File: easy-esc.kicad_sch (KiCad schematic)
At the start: 43 parts, among them J101 USB_C_Receptacle_USB2.0, J102 BLDC, J103 POWER, SW101 BOOT, SW102 RESET, SW103 EN, U101 TMC6300, U102 XC6206, U103 W25Q128JVS, U104 RP2040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

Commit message: finalize fab files
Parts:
- added C113: 100uF, Capacitor_SMD:CP_Elec_4x3.9, symbol Device:C_Polarized_US
- added H101: PCB, matei:easy-esc-outline, symbol Mechanical:MountingHole_Pad
- added R113, R114: 0, Resistor_SMD:R_0402_1005Metric, symbol Device:R_Small_US
- added U105, U106: INA180A1, Package_TO_SOT_SMD:SOT-23-5, symbol Amplifier_Current:INA180A1
- R105, R106: footprint Resistor_SMD:R_0402_1005Metric -> Resistor_SMD:R_2512_6332Metric
- TP101, TP102, TP103, TP104, TP105: footprint TestPoint:TestPoint_Loop_D1.80mm_Drill1.0mm_Beaded -> TestPoint:TestPoint_Pad_D1.5mm
- U101: footprint Package_DFN_QFN:QFN-20-1EP_3x3mm_P0.4mm_EP1.65x1.65mm_ThermalVias -> Package_DFN_QFN:QFN-20-1EP_3x3mm_P0.4mm_EP1.65x1.65mm
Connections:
- net +3V3: now also U105.5 (V+), U106.5 (V+)
- net +5V: now also C113.1
- net GND: now also U101.21 (PAD), C113.2, H101.1, R113.2, R114.2, U105.2 (GND), U105.4 (-), U106.2 (GND), U106.4 (-); no longer U101.PAD
- net UVSENSE: now also R114.1, U106.3 (+); no longer U104.39 (GPIO27/ADC1)
- net WSENSE: now also R113.1, U105.3 (+); no longer U104.38 (GPIO26/ADC0)
- new net UVCUR: U104.39 (GPIO27/ADC1), U106.1
- new net WCUR: U104.38 (GPIO26/ADC0), U105.1
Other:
- note added: "BOARD"
- moved on the sheet: C101, C102, C103, C104, C105, D101, J102, R101, R102, R105, R106, SW103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

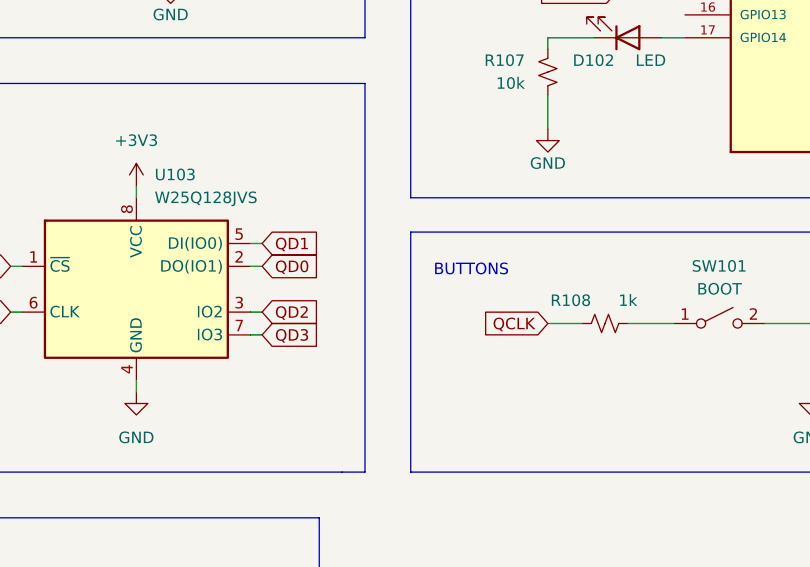
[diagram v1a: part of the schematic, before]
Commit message: fix schematic and layout issues from V1 production run
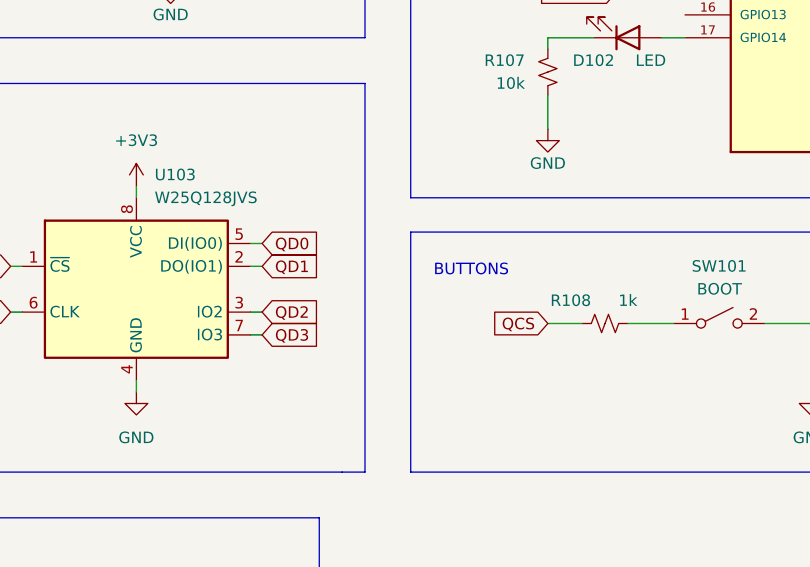
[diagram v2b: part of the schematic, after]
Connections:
- net QCLK: no longer R108.1
- net QCS: now also R108.1
- net QD0: now also U103.5 (DI(IO0)); no longer U103.2 (DO(IO1))
- net QD1: now also U103.2 (DO(IO1)); no longer U103.5 (DI(IO0))
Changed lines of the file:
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@@
     )
   )
-  (global_label "QCLK" (shape input) (at 198.12 144.78 180) (fields_autoplaced)
+  (global_label "QCS" (shape input) (at 198.12 144.78 180) (fields_autoplaced)
     (effects (font (size 1.27 1.27)) (justify right))
-    (property "Intersheet References" "${INTERSHEET_REFS}" (id 0) (at 190.8083 144.7006 0)
+    (property "Intersheet References" "${INTERSHEET_REFS}" (id 0) (at 191.8969 144.7006 0)
       (effects (font (size 1.27 1.27)) (justify right) hide)
     )
@@
     )
   )
-  (global_label "QD1" (shape input) (at 166.37 135.89 0) (fields_autoplaced)
+  (global_label "QD1" (shape input) (at 166.37 138.43 0) (fields_autoplaced)
     (effects (font (size 1.27 1.27)) (justify left))
-    (property "Intersheet References" "${INTERSHEET_REFS}" (id 0) (at 172.5931 135.8106 0)
+    (property "Intersheet References" "${INTERSHEET_REFS}" (id 0) (at 172.5931 138.3506 0)
       (effects (font (size 1.27 1.27)) (justify left) hide)
     )
@@
     )
   )
-  (global_label "QD0" (shape input) (at 166.37 138.43 0) (fields_autoplaced)
+  (global_label "QD0" (shape input) (at 166.37 135.89 0) (fields_autoplaced)
     (effects (font (size 1.27 1.27)) (justify left))
-    (property "Intersheet References" "${INTERSHEET_REFS}" (id 0) (at 172.5931 138.3506 0)
+    (property "Intersheet References" "${INTERSHEET_REFS}" (id 0) (at 172.5931 135.8106 0)
       (effects (font (size 1.27 1.27)) (justify left) hide)
     )

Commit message: Auto-commit Tue Apr 11 10:47:13 EDT 2023
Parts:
- R107: value 10k -> 1k
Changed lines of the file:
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@@
       (effects (font (size 1.27 1.27)) (justify right))
     )
-    (property "Value" "10k" (id 1) (at 195.58 118.1099 0)
+    (property "Value" "1k" (id 1) (at 195.58 118.1099 0)
       (effects (font (size 1.27 1.27)) (justify right))
     )
@@
     )
     (path "/986fd365-1496-494b-911d-7d7788ddbcba"
-      (reference "R107") (unit 1) (value "10k") (footprint "Resistor_SMD:R_0402_1005Metric")
+      (reference "R107") (unit 1) (value "1k") (footprint "Resistor_SMD:R_0402_1005Metric")
     )
     (path "/a02a4c82-9ae4-4628-bd1b-9900d4169020"
